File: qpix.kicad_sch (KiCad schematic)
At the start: 93 parts, among them J1 Conn_01x32, J13 DigReset, J2 Conn_01x09, J3 TxRx_D, J4 TxRx_A, J5 SPI, J6 TxRx_B, J8 TxRx_C, J9 Conn_Coaxial_Power, Q1 Q, Q2 Q, Q3 Q, Q4 Q, U1 qpix_digital

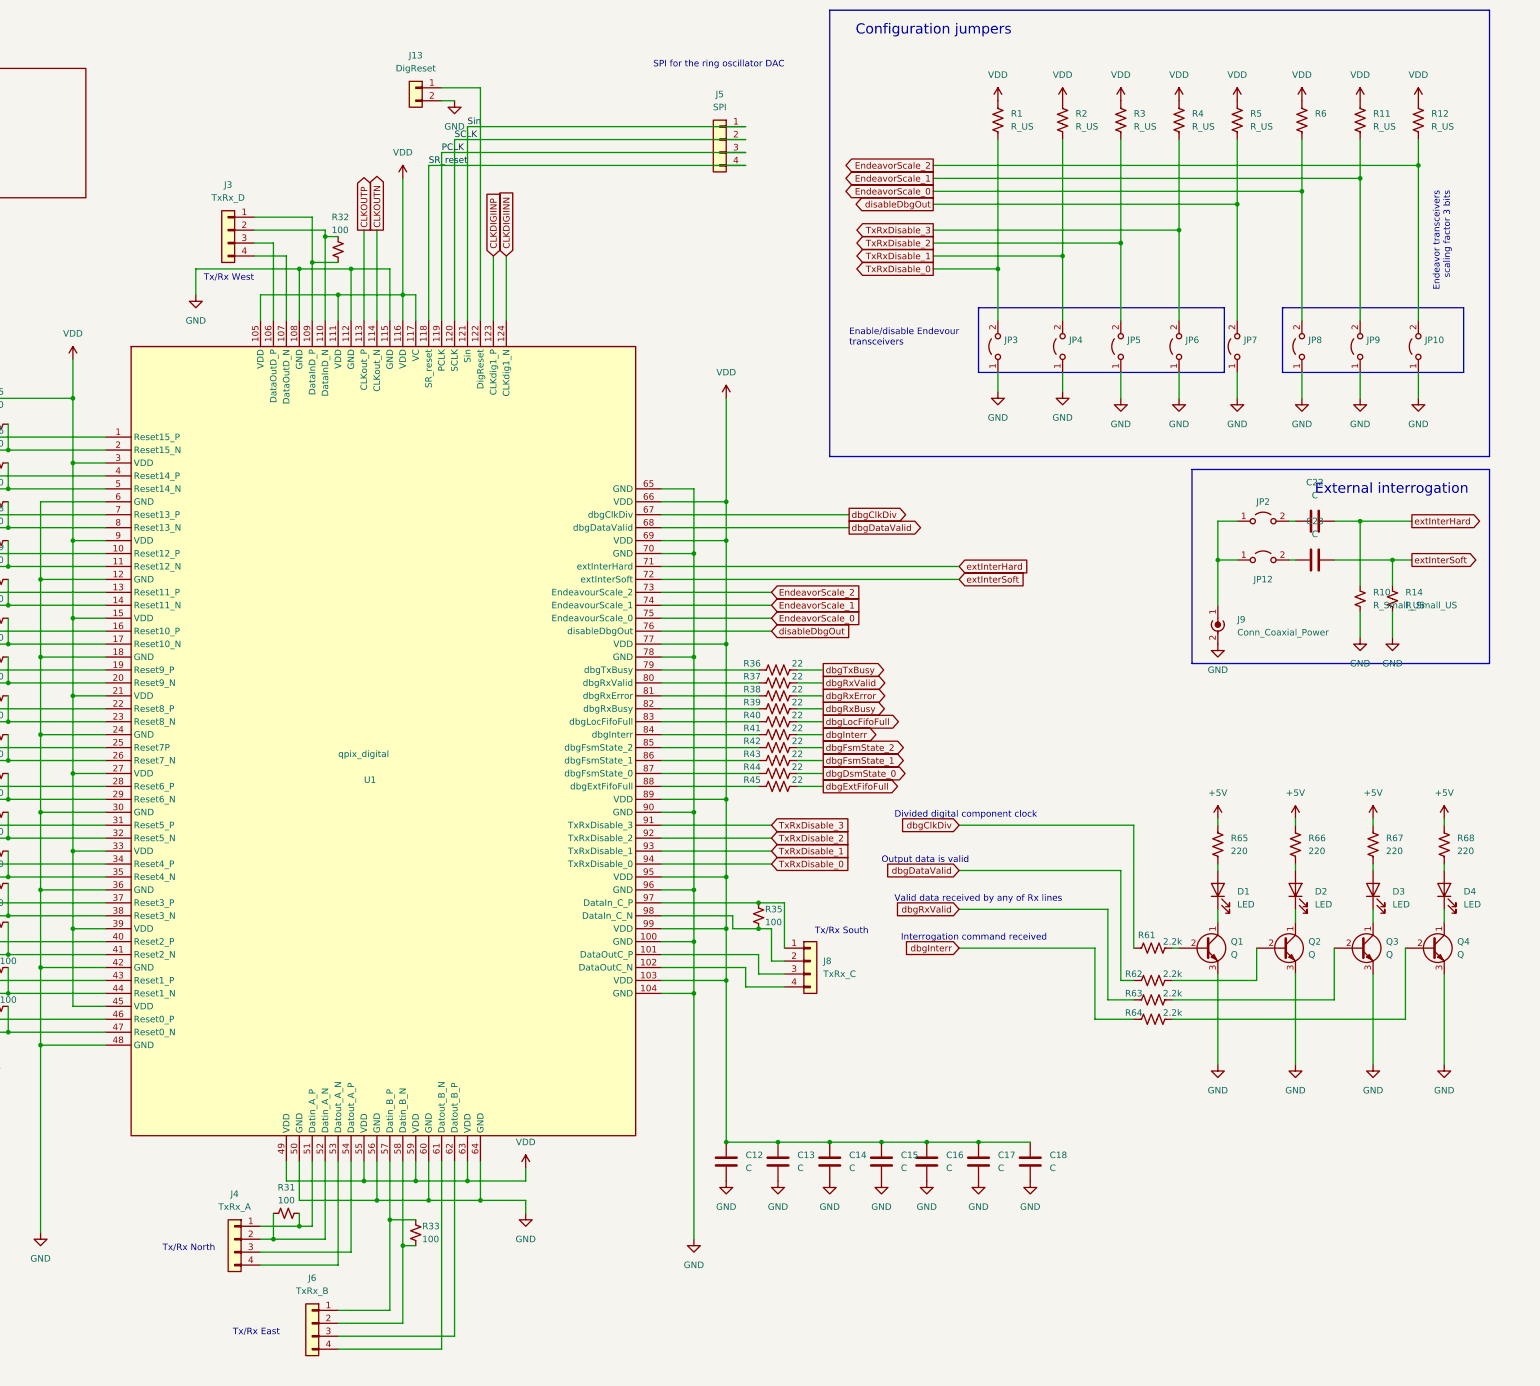
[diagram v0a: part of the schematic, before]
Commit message: add a footprint for QPix ASIC CoB  and its generator
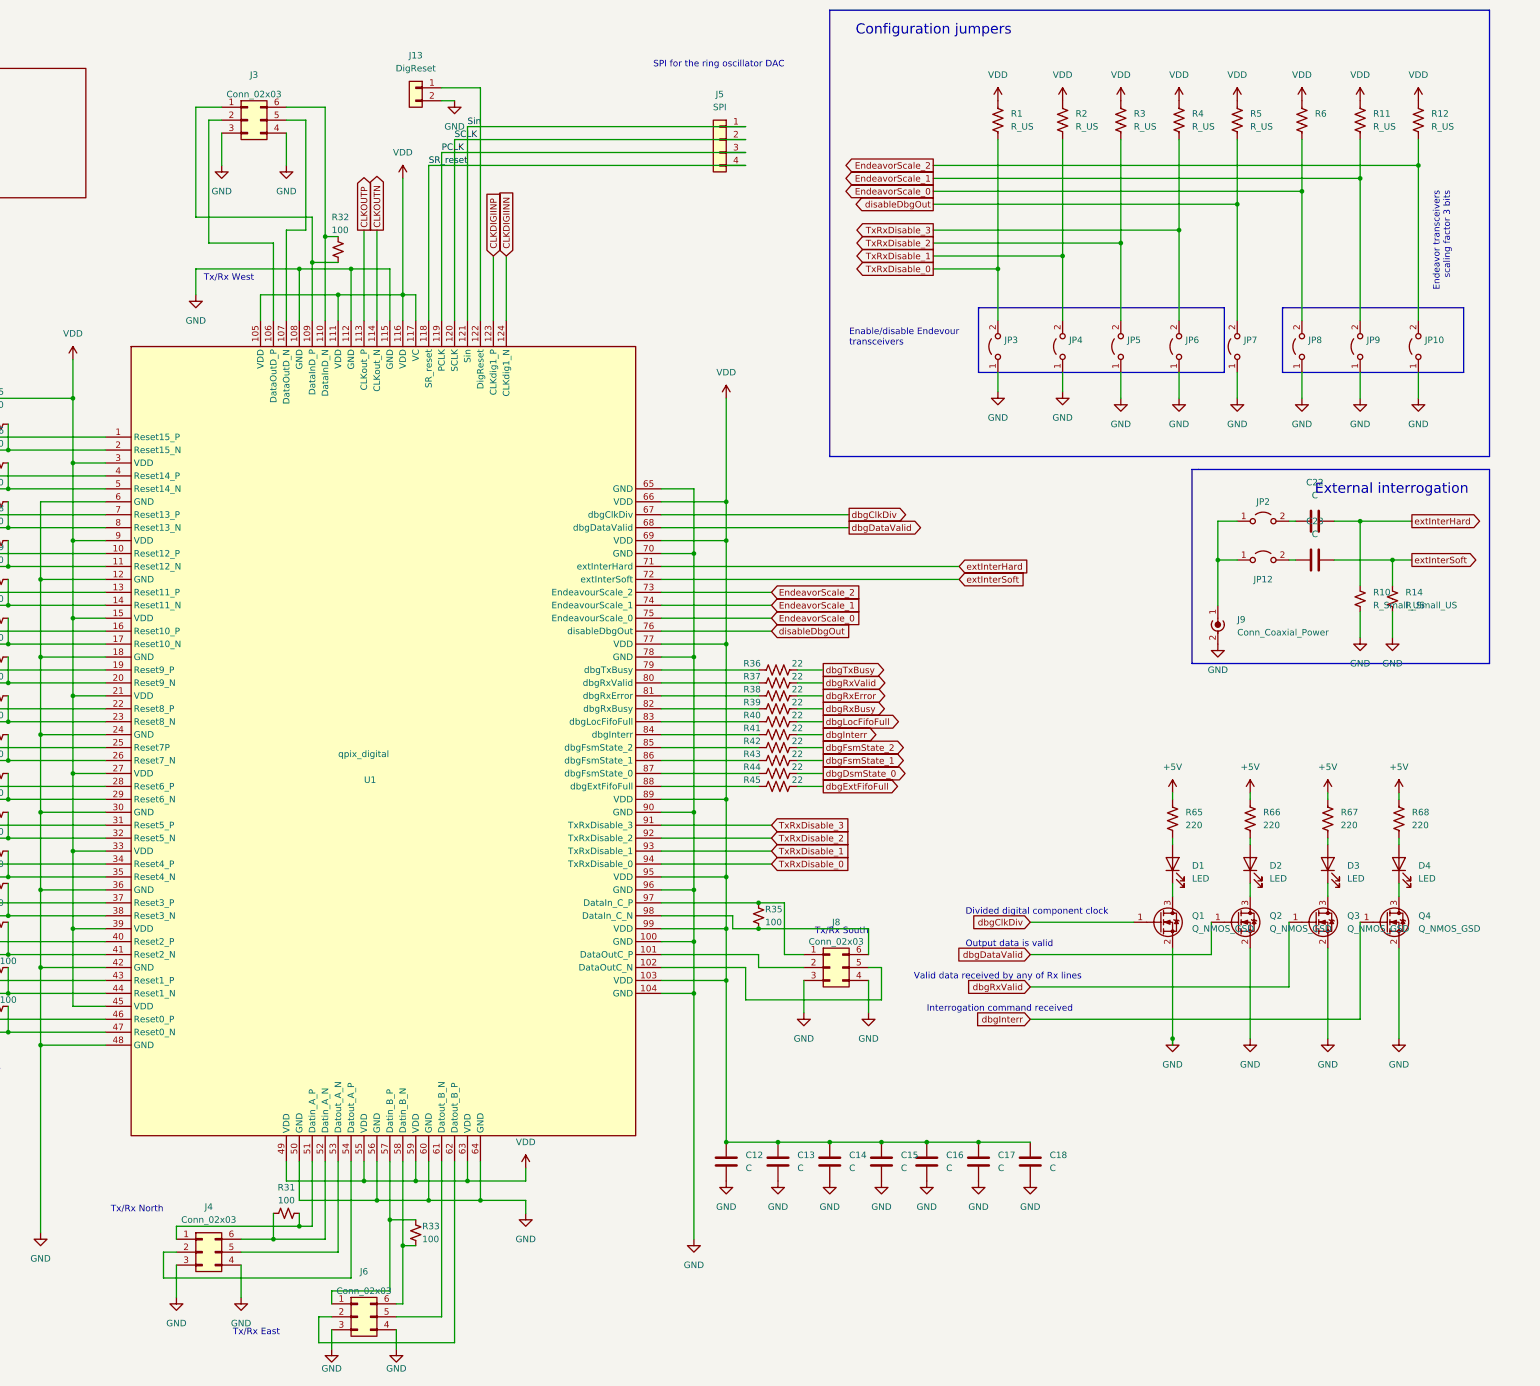
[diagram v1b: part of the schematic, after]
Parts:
- removed J3: TxRx_D, Connector_PinSocket_2.54mm:PinSocket_1x04_P2.54mm_Horizontal, symbol Connector_Generic:Conn_01x04
- removed J4: TxRx_A, Connector_PinSocket_2.54mm:PinSocket_1x04_P2.54mm_Horizontal, symbol Connector_Generic:Conn_01x04
- removed J6: TxRx_B, Connector_PinSocket_2.54mm:PinSocket_1x04_P2.54mm_Horizontal, symbol Connector_Generic:Conn_01x04
- removed J8: TxRx_C, Connector_PinSocket_2.54mm:PinSocket_1x04_P2.54mm_Horizontal, symbol Connector_Generic:Conn_01x04
- removed Q1, Q2, Q3, Q4: Q, Package_TO_SOT_SMD:SOT-23, symbol Device:Q_NPN_CBE
- removed R61, R62, R63, R64: 2.2k, Resistor_SMD:R_0603_1608Metric, symbol Device:R_US
- added J3, J4, J6, J8: Conn_02x03, Connector_PinSocket_1.27mm:PinSocket_2x03_P1.27mm_Horizontal, symbol Connector_Generic:Conn_02x03_Counter_Clockwise
- added Q1, Q2, Q3, Q4: Q_NMOS_GSD, Package_TO_SOT_SMD:SOT-323_SC-70, symbol Device:Q_NMOS_GSD
- J9: footprint Connector_Coaxial:BNC_TEConnectivity_1478035_Horizontal -> Connector_Coaxial:SMA_Amphenol_901-144_Vertical
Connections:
- net GND: now also J3.3 (Pin_3), J3.4 (Pin_4), J4.3 (Pin_3), J4.4 (Pin_4), J6.3 (Pin_3), J6.4 (Pin_4), J8.3 (Pin_3), J8.4 (Pin_4), Q1.2 (S), Q2.2 (S), Q3.2 (S), Q4.2 (S)
- net dbgClkDiv: now also Q1.1 (G)
- net dbgDataValid: now also Q2.1 (G)
- net dbgInterr: now also Q4.1 (G)
- net dbgRxValid: now also Q3.1 (G)
- net at D4.1 (K): now also Q4.3 (D)
- net at D3.1 (K): now also Q3.3 (D)
- net at R31.1, U1.51 (Datin_A_P): now also J4.1 (Pin_1)
- net at R31.2, U1.52 (Datin_A_N): now also J4.6 (Pin_6)
- net at R35.2, U1.97 (DataIn_C_P): now also J8.1 (Pin_1)
- net at R35.1, U1.98 (DataIn_C_N): now also J8.6 (Pin_6)
- net at U1.101 (DataOutC_P): now also J8.2 (Pin_2)
- net at U1.102 (DataOutC_N): now also J8.5 (Pin_5)
- net at D1.1 (K): now also Q1.3 (D)
- net at R33.2, U1.57 (Datin_B_P): now also J6.1 (Pin_1)
- net at R33.1, U1.58 (Datin_B_N): now also J6.6 (Pin_6)
- net at U1.62 (Datout_B_P): now also J6.2 (Pin_2)
- net at U1.61 (Datout_B_N): now also J6.5 (Pin_5)
- net at D2.1 (K): now also Q2.3 (D)
- net at U1.106 (DataOutD_P): now also J3.2 (Pin_2)
- net at U1.107 (DataOutD_N): now also J3.5 (Pin_5)
- net at R32.1, U1.109 (DataInD_P): now also J3.1 (Pin_1)
- net at R32.2, U1.110 (DataInD_N): now also J3.6 (Pin_6)
- net at U1.53 (Datout_A_N): now also J4.5 (Pin_5)
- net at U1.54 (Datout_A_P): now also J4.2 (Pin_2)
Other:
- moved on the sheet: D1, D2, D3, D4, R65, R66, R67, R68

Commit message: some progress in routing
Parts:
- U1: footprint Package_QFP:TQFP-144_20x20mm_P0.5mm -> qpix-digi-pcb:qpix_digi_footprint
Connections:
- net DatinA_P: now reaches J4.1 (Pin_1), R31.1, U1.51 (DatinA_P)
- net DatinA_N: now reaches J4.6 (Pin_6), R31.2, U1.52 (DatinA_N)
- net DatinB_N: now reaches R33.1, U1.58 (DatinB_N)
- net DatinB_N: now also J6.2 (Pin_2); no longer J6.6 (Pin_6)
- net DatinB_P: now reaches J6.1 (Pin_1), R33.2, U1.57 (DatinB_P)
- net DatoutA_N: now reaches J4.5 (Pin_5), U1.53 (DatoutA_N)
- net DatoutA_P: now reaches J4.2 (Pin_2), U1.54 (DatoutA_P)
- net DatoutB_N: now reaches U1.61 (DatoutB_N)
- net DatoutB_N: now also J6.6 (Pin_6); no longer J6.5 (Pin_5)
- net DatoutB_P: now reaches U1.62 (DatoutB_P)
- net DatoutB_P: now also J6.5 (Pin_5); no longer J6.2 (Pin_2)
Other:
- moved on the sheet: J4, J6, R33

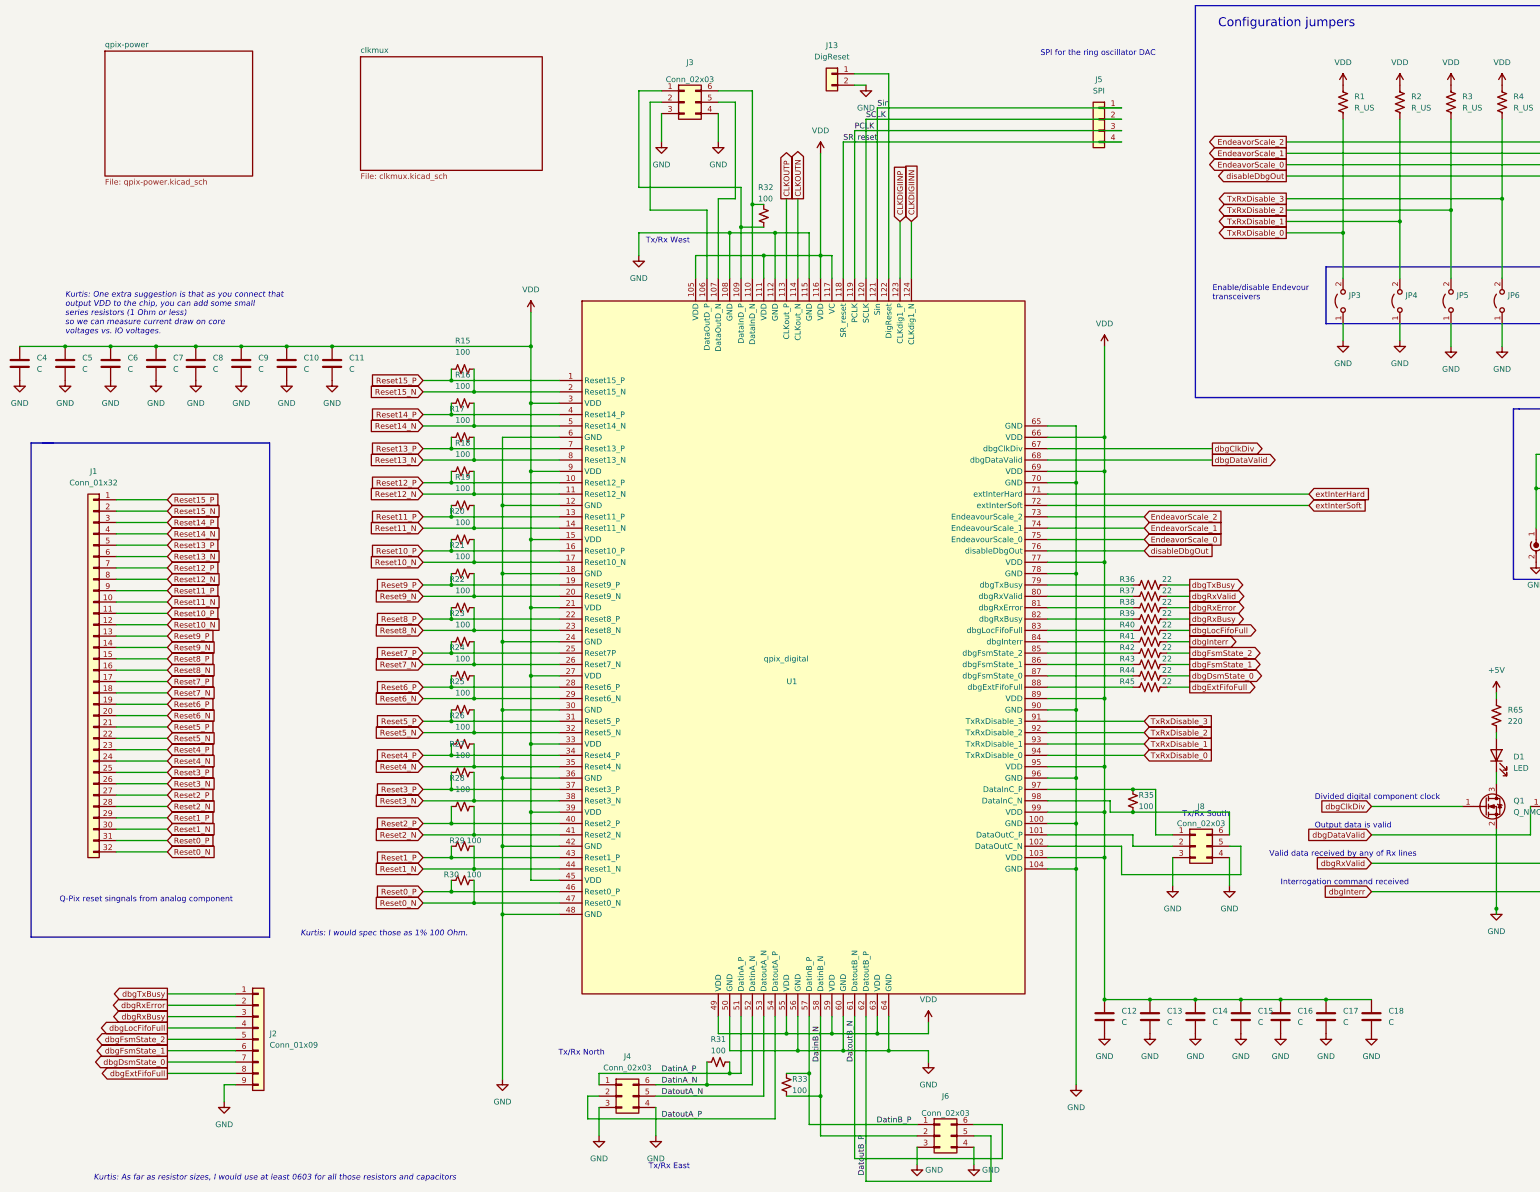
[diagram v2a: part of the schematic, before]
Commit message: the board is fully routed for the first time
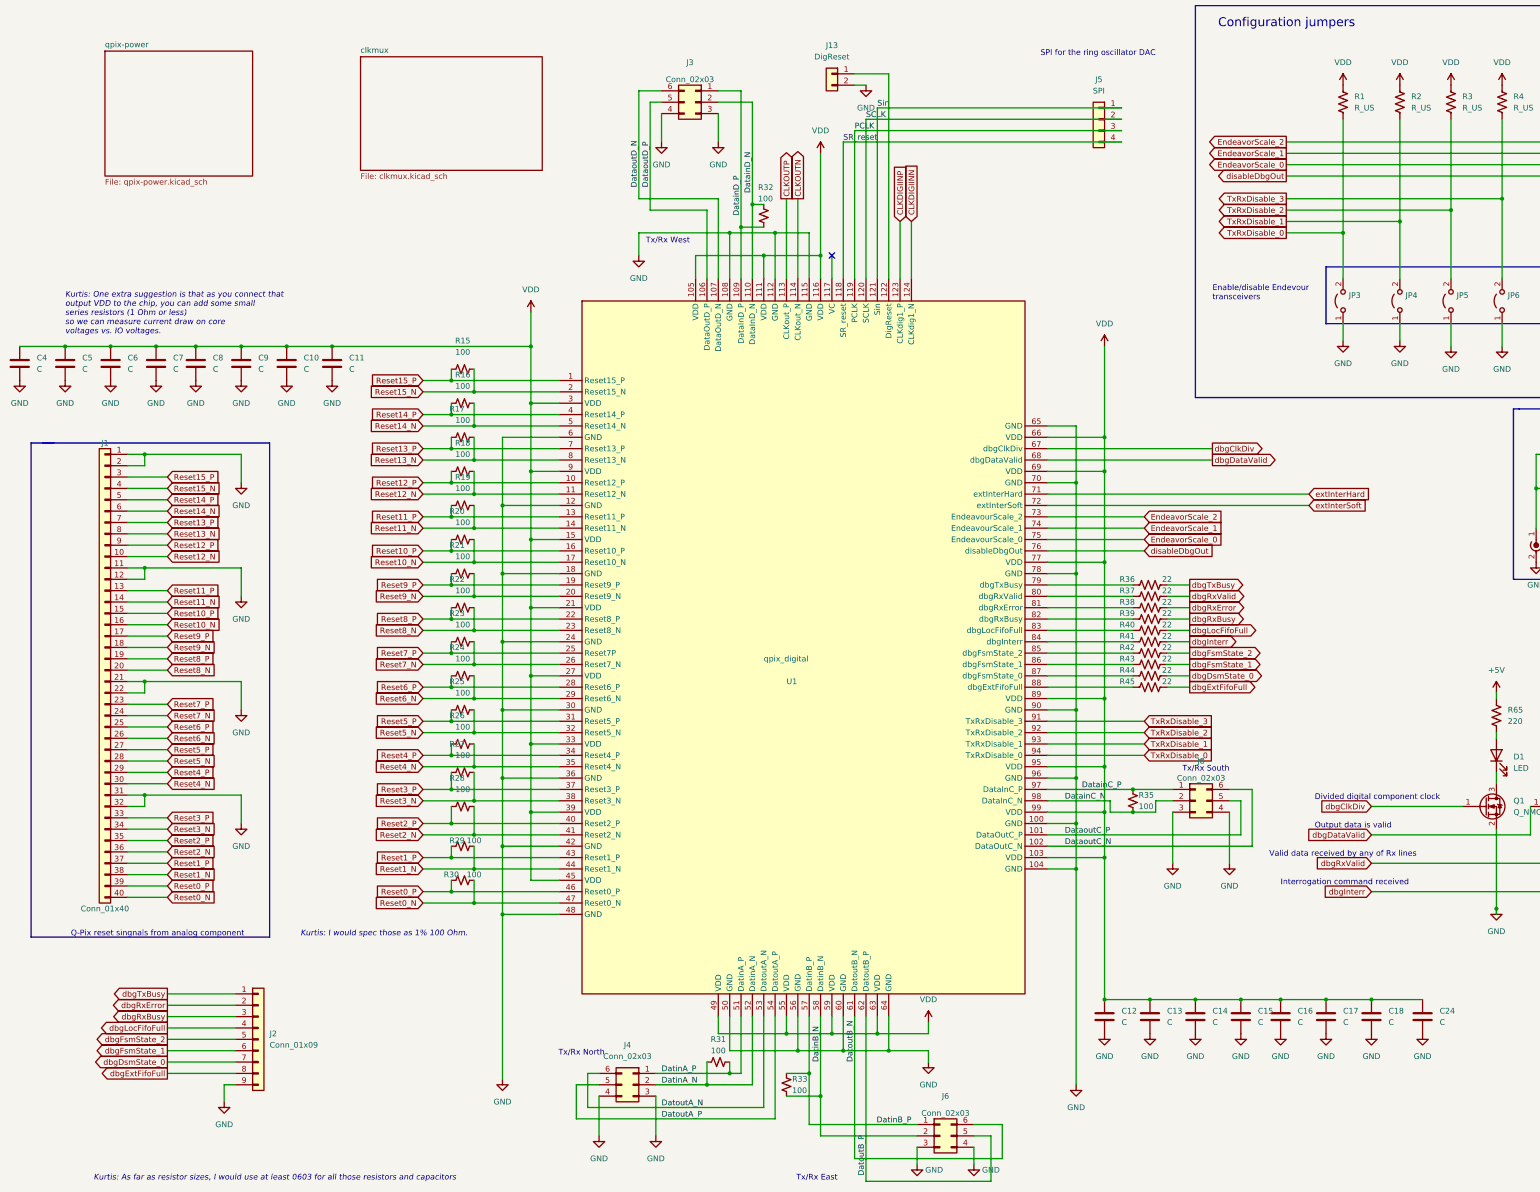
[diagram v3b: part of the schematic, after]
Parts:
- removed J1: Conn_01x32, Connector_PinHeader_2.54mm:PinHeader_2x16_P2.54mm_Vertical, symbol Connector_Generic:Conn_01x32
- added C24: C, Capacitor_SMD:C_0603_1608Metric, symbol Device:C
- added J1: Conn_01x40, Connector_PinHeader_2.54mm:PinHeader_2x20_P2.54mm_Vertical, symbol Connector_Generic:Conn_01x40
- J3, J4, J6, J8: footprint Connector_PinSocket_1.27mm:PinSocket_2x03_P1.27mm_Horizontal -> Connector_PinSocket_2.54mm:PinSocket_2x03_P2.54mm_Horizontal
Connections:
- net DatinA_N: now also J4.2 (Pin_2); no longer J4.6 (Pin_6)
- net DatoutA_N: now also J4.6 (Pin_6); no longer J4.5 (Pin_5)
- net DatoutA_P: now also J4.5 (Pin_5); no longer J4.2 (Pin_2)
- net GND: now also C24.2, J1.1 (Pin_1), J1.11 (Pin_11), J1.12 (Pin_12), J1.2 (Pin_2), J1.21 (Pin_21), J1.22 (Pin_22), J1.31 (Pin_31), J1.32 (Pin_32)
- net Reset0_N: now also J1.40 (Pin_40)
- net Reset0_P: now also J1.39 (Pin_39)
- net Reset10_N: now also J1.16 (Pin_16)
- net Reset10_P: now also J1.15 (Pin_15)
- net Reset11_N: now also J1.14 (Pin_14)
- net Reset11_P: now also J1.13 (Pin_13)
- net Reset12_N: now also J1.10 (Pin_10)
- net Reset12_P: now also J1.9 (Pin_9)
- net Reset13_N: now also J1.8 (Pin_8)
- net Reset13_P: now also J1.7 (Pin_7)
- net Reset14_N: now also J1.6 (Pin_6)
- net Reset14_P: now also J1.5 (Pin_5)
- net Reset15_N: now also J1.4 (Pin_4)
- net Reset15_P: now also J1.3 (Pin_3)
- net Reset1_N: now also J1.38 (Pin_38)
- net Reset1_P: now also J1.37 (Pin_37)
- net Reset2_N: now also J1.36 (Pin_36)
- net Reset2_P: now also J1.35 (Pin_35)
- net Reset3_N: now also J1.34 (Pin_34)
- net Reset3_P: now also J1.33 (Pin_33)
- net Reset4_N: now also J1.30 (Pin_30)
- net Reset4_P: now also J1.29 (Pin_29)
- net Reset5_N: now also J1.28 (Pin_28)
- net Reset5_P: now also J1.27 (Pin_27)
- net Reset6_N: now also J1.26 (Pin_26)
- net Reset6_P: now also J1.25 (Pin_25)
- net Reset7_N: now also J1.24 (Pin_24)
- net Reset7_P: now also J1.23 (Pin_23)
- net Reset8_N: now also J1.20 (Pin_20)
- net Reset8_P: now also J1.19 (Pin_19)
- net Reset9_N: now also J1.18 (Pin_18)
- net Reset9_P: now also J1.17 (Pin_17)
- net VDD: now also C24.1; no longer U1.117 (VC)
- net DatainC_N: now reaches J8.2 (Pin_2)
- net DatainC_N: now also R35.1, U1.98 (DataInC_N); no longer U1.101 (DataOutC_P)
- net DataoutC_N: now reaches U1.102 (DataOutC_N)
- net DataoutC_N: now also J8.6 (Pin_6); no longer J8.5 (Pin_5)
- net DatainD_N: now reaches J3.2 (Pin_2)
- net DatainD_N: now also R32.2, U1.110 (DataInD_N); no longer U1.106 (DataOutD_P)
- net DataoutD_N: now reaches U1.107 (DataOutD_N)
- net DataoutD_N: now also J3.6 (Pin_6); no longer J3.5 (Pin_5)
- net DatainD_P: now reaches J3.1 (Pin_1), R32.1, U1.109 (DataInD_P)
- net DatainC_P: now reaches J8.1 (Pin_1), R35.2, U1.97 (DataInC_P)
- new net DataoutC_P: J8.5 (Pin_5), U1.101 (DataOutC_P)
- new net DataoutD_P: J3.5 (Pin_5), U1.106 (DataOutD_P)
- no-connect marks 0 -> 1
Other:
- moved on the sheet: J4, J8
